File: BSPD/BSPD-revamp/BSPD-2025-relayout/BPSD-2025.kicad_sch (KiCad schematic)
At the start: 61 parts, among them J1 SAMMY-3PIN, J2 SAMMY-3PIN, J3 SAMMY-2PIN, J4 SAMMY-5PIN, J5 SAMMY-2PIN, Q1 NMOS, U10 LM397, U11 SN74AHC1G08DBVR, U12 LM397, U17 SN74AHC1G32DBVR, U18 SN74AHC1G32DBVR, U3 LM1117DT-5.0, U4 LM397, U5 LM397, U6 LM397, U7 SN74AHC1G08DBVR, U8 SN74AHC1G00DBVR, U9 LM397

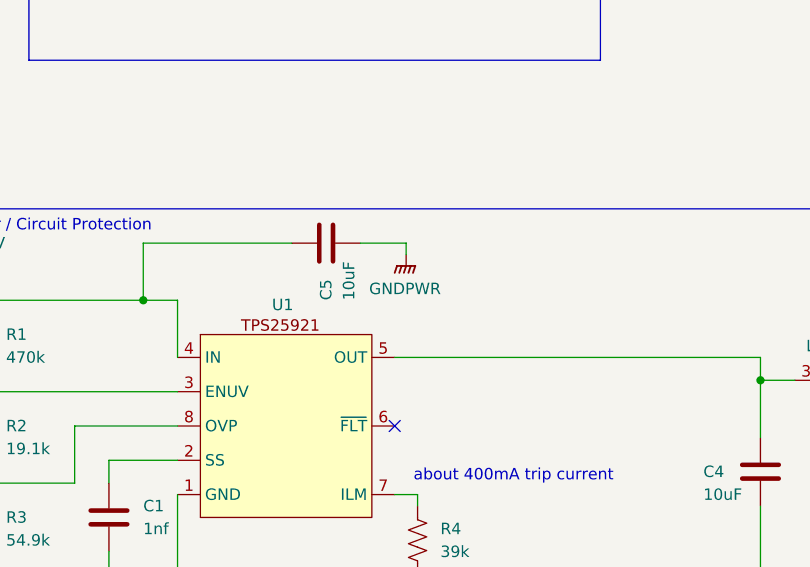
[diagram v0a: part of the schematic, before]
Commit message: Reroute BSPD and adjust connector spacing
The other routing was atrocious. Also regenerated gerbers, drills, and 3d model.
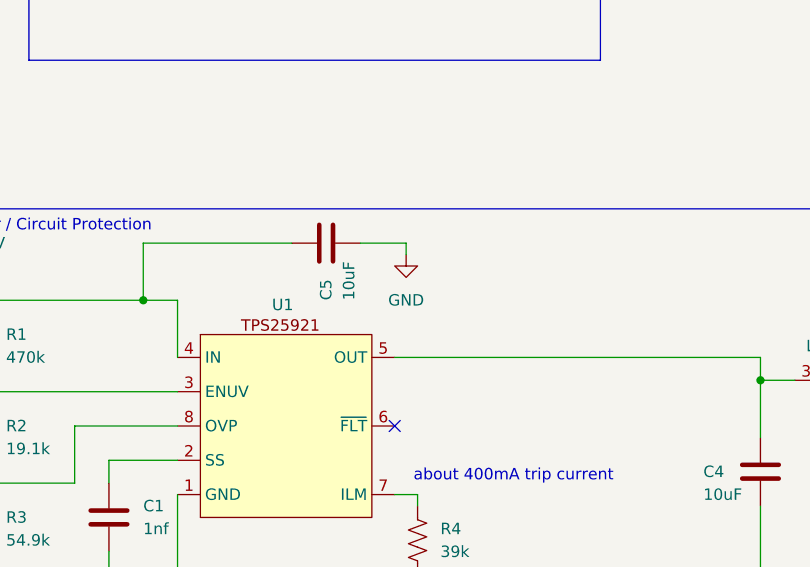
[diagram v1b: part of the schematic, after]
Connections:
- net GNDPWR is gone; now on net GND: C5.2

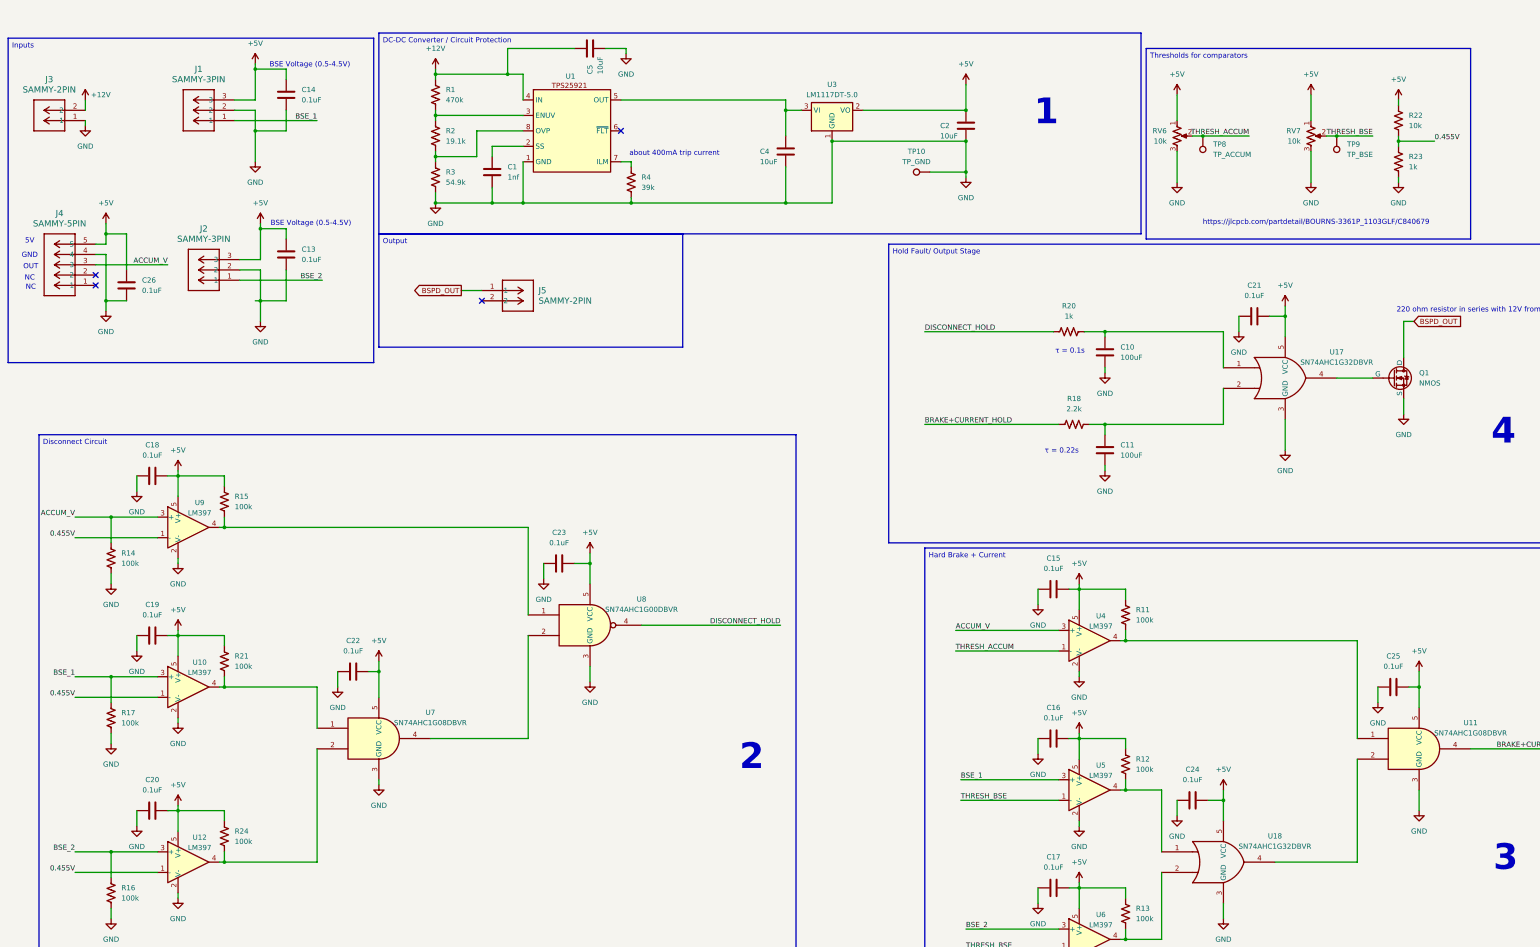
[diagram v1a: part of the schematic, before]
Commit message: Connectors, time delay, vreferences
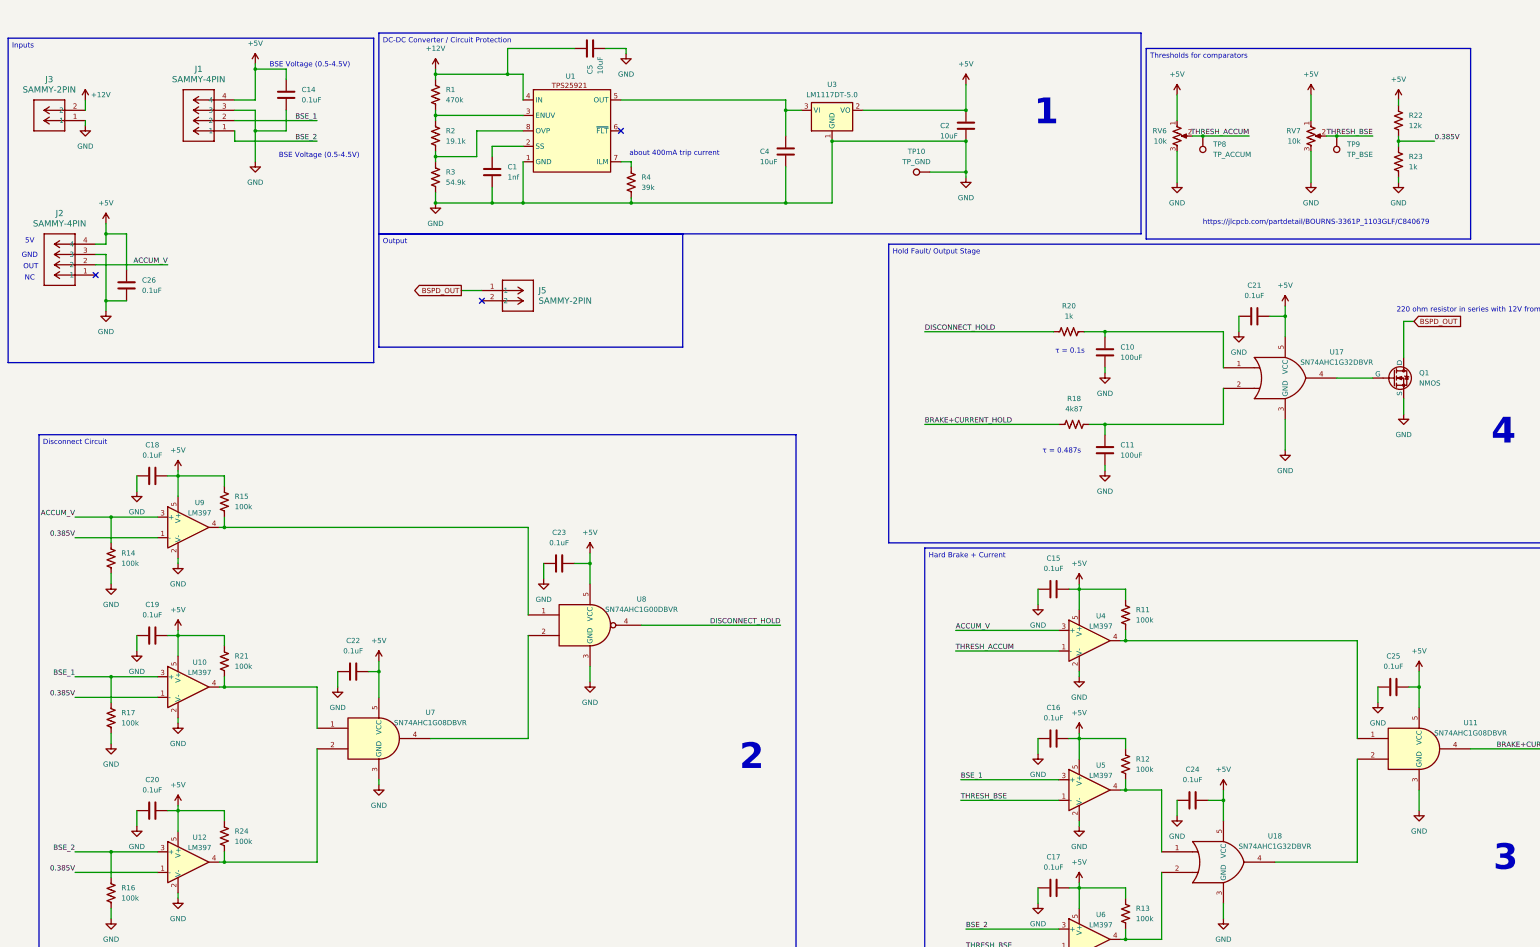
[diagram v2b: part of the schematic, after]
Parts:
- removed C13: 0.1uF, Capacitor_SMD:C_1206_3216Metric, symbol Device:C
- removed J1, J2: SAMMY-3PIN, BSPD:SAMMY-3PIN, symbol BSPD:SAMMY-3PIN
- removed J4: SAMMY-5PIN, BSPD:SAMMY-5PIN, symbol BSPD:SAMMY-5PIN
- added J1, J2: SAMMY-4PIN, BSPD:SAMMY-4PIN, symbol BSPD:SAMMY-4PIN
- R18: value 2.2k -> 4k87; JLC# C230160 -> C230270
- R22: value 10k -> 12k; JLC# C309586 -> C182355
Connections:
- net +5V: now also J1.4, J2.4
- net ACCUM_V: now also J2.2
- net BSE_1: now also J1.2
- net BSE_2: now also J1.1
- net GND: now also J1.3, J2.3
- net 0.455V renamed 0.385V
- no-connect marks 4 -> 3
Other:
- note added: "τ = 0.487s"
- note removed: "τ = 0.22s"

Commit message: BSPD, Precharge, and Charging PCB BOMs pulled
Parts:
- C14, C15, C16, C17, C18, C19, C20, C21, C22, C23, C24, C25, C26: JLC# C1945 -> C24497
- R11, R12, R13, R14, R15, R16, R17, R21, R24: JLC# C230004 -> C185765
- R18: JLC# C230270 -> C3000590
